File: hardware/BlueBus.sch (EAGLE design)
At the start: 72 parts

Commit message: [FIX] hardware: BlueBus v7 * Update Silkscreen for Speaker outputs * Rewire Speaker negative outputs to support single ended operation without overheating * Place 10uF cap for TPA6017A2 near input of 5v so all VDDs can benefit from it * Connect TPA6017A2 N/C pin to GND * Move TPA6017A2 gain resistor * Rewire transient filter for BC127 on the 3.3v rail per application note * Update placement of several passives for alignment * Update passive names to move from bottom right to left, to top right to left * Update Silkscreen with GitHub address
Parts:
- removed R21: 240, Passives:240OHM
- added C28, C29: 0.47uF, Passives:0.47UF
- added C30: 4.7uF, Passives:4.7UF
- added C31: 100nF, Passives:100NF
- C1: value 0.1uF -> 100uF; device Passives:0.1UF -> Passives:100UF2917
- C10: value 47nF -> 0.1uF; device Passives:47NF -> Passives:0.1UF
- C11: value 0.01uF -> 0.1uF; device Passives:0.01UF -> Passives:0.1UF
- C12: value 10uF -> 0.1uF; device Passives:10UF -> Passives:0.1UF
- C13: value 0.47uF -> 10uF; device Passives:0.47UF -> Passives:10UF
- C14, C16, C17, C18: value 0.47uF -> 0.1uF; device Passives:0.47UF -> Passives:0.1UF
- C15: value 10uF -> 2.2uF; device Passives:10UF -> Passives:2.2UF
- C19, C20: value 0.47uF -> (none); device Passives:0.47UF -> Passives:10UF2012
- C2: value 0.1uF -> 47nF; device Passives:0.1UF -> Passives:47NF
- C21: value 22uF -> (none); device Passives:22UF -> Passives:10UF2012
- C22, C23, C24, C27: value 0.1uF -> 0.47uF; device Passives:0.1UF -> Passives:0.47UF
- C25, C3: value 0.1uF -> 10uF; device Passives:0.1UF -> Passives:10UF
- C26: value 10uF -> 0.47uF; device Passives:10UF -> Passives:0.47UF
- C4: value 0.1uF -> 22uF; device Passives:0.1UF -> Passives:22UF
- C7: value 4.7uF -> 0.01uF; device Passives:4.7UF -> Passives:0.01UF
- C8: value 2.2uF -> 0.1uF; device Passives:2.2UF -> Passives:0.1UF
- C9: value 100uF -> 0.1uF; device Passives:100UF2917 -> Passives:0.1UF
- D3: value GREEN-0805 -> 2A/100V; device Seeed-LED:SMD-LED-CLEAR-GREEN(0805) -> Passives:SCHOTTKYDIODE2A30V
- D5: value RED-0805 -> GREEN-0805; device Seeed-LED:SMD-LED-CLEAR-RED(0805) -> Seeed-LED:SMD-LED-CLEAR-GREEN(0805)
- D6: value 2A/100V -> RED-0805; device Passives:SCHOTTKYDIODE2A30V -> Seeed-LED:SMD-LED-CLEAR-RED(0805)
- R1: value 0.22 -> 100k; device Passives:0.22OHM -> Passives:100KOHM0805
- R10: value 100k -> 10k; device Passives:100KOHM0805 -> Passives:10KOHM0805
- R11, R12: value 100k -> 1k; device Passives:100KOHM0805 -> Passives:1KOHM
- R13: value 100k -> 36k; device Passives:100KOHM0805 -> Passives:36KOHM2012
- R14: value 1k -> 2k; device Passives:1KOHM -> Passives:2KOHM0805
- R15: value 1k -> 100k; device Passives:1KOHM -> Passives:100KOHM0805
- R16: value 10k -> 100k; device Passives:10KOHM0805 -> Passives:100KOHM0805
- R17: value 5.1k -> 10k; device Passives:5.1KOHM0805 -> Passives:10KOHM0805
- R18: value 36k -> 10k; device Passives:36KOHM2012 -> Passives:10KOHM0805
- R19: value 2k -> 10k; device Passives:2KOHM0805 -> Passives:10KOHM0805
- R2: value 0.75 -> 47k; device Passives:0.75OHM -> Passives:47KOHM
- R3: value 10k -> 9.09k; device Passives:10KOHM0805 -> Passives:9.09KOHM
- R4: value 10k -> 2k; device Passives:10KOHM0805 -> Passives:2KOHM0805
- R5: value 10k -> 240; device Passives:10KOHM0805 -> Passives:240OHM
- R7: value 47k -> 5.1k; device Passives:47KOHM -> Passives:5.1KOHM0805
- R8: value 9.09k -> 100k; device Passives:9.09KOHM -> Passives:100KOHM0805
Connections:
- removed net BT_VBAT: BC127.VBAT, R1.2, R2.1
- removed net SPKR_OUT_NEG: SPKR_OUT.2, SPKR_OUT.4, TPA6017A2.LOUT-, TPA6017A2.ROUT-
- removed net VBAT_CAP: C7.1, R1.1
- new net BT_VCHG: BC127.VCHG, C30.1, R4.1
- new net SPKR_OUT_GND: C19.2, C20.2, C21.2, SPKR_OUT.3, SPKR_OUT.4
- new net SPKR_OUT_LN: C21.1, TPA6017A2.LOUT-
- new net SPKR_OUT_RN: C19.1, TPA6017A2.ROUT-
- net 3.3V: now also BC127.VBAT, C10.1, C11.1, C16.1, C17.1, C18.1, C31.1, C8.1, C9.1, D6.+, R10.1, R17.1, R19.2, R4.2, R7.2, R8.1, R9.1; no longer BC127.VCHG, C1.1, C2.1, C22.1, C23.1, C24.1, C3.1, C4.1, D4.+, R12.1, R13.1, R16.1, R17.2, R2.2, R20.1, R3.2
- net 5V: now also C22.1, C23.1, C25.1, C4.1, D3.C, R15.1, R16.2, R2.1, R20.2; no longer C13.1, C14.1, C15.1, C21.1, D6.C, R10.1, R11.2, R4.2, R7.1
- net BS: now also C7.2; no longer C11.2
- net BT_RESET: now also R17.2; no longer R6.2
- net BT_URX: now also R18.1, R18.2; no longer R5.1, R5.2
- net BT_UTX: now also R19.1, R20.1; no longer R3.1, R4.1
- net BYP: now also C24.1; no longer C20.1
- net EE_CS: now also R7.1; no longer R17.1
- net EN: now also R1.2; no longer R9.2
- net FB: now also R2.2, R3.2; no longer R7.2, R8.2
- net GAIN1: now also R15.2; no longer R10.2
- net GND: now also C11.2, C16.2, C17.2, C18.2, C20.1, C30.2, C31.2, R14.2, R3.1, TPA6017A2.NC; no longer C20.2, C21.2, C26.2, C27.2, C7.2, R19.2, R8.1
- net MCP_5V: now also D3.A; no longer D6.A
- net MCP_LED0: now also R12.1; no longer R15.1
- net MCP_LED0_RES: now also D6.-, R12.2; no longer D5.-, R15.2
- net MCP_LED1: now also R11.1; no longer R14.1
- net MCP_LED1_RES: now also D5.-, R11.2; no longer D4.-, R14.2
- net MCP_RESET: now also R10.2; no longer R16.2
- net MCU_MCLR: now also R5.2; no longer R21.2
- net MCU_MCLR_PULL_UP: now also C12.1, R5.1, R6.2; no longer C27.1, R20.2, R21.1
- net ON_LED: now also D4.+, R13.1; no longer D3.+, R18.1
- net ON_LED_RES: now also D4.-, R13.2, R14.1; no longer D3.-, R18.2, R19.1
- net SHDN: now also R16.1; no longer R11.1
- net SPKR_IN_LN: now also C27.1, C27.2; no longer C16.1, C16.2
- net SPKR_IN_LP: now also C28.1, C28.2; no longer C18.1, C18.2
- net SPKR_IN_RN: now also C26.1, C26.2; no longer C19.1, C19.2
- net SPKR_IN_RP: now also C29.1, C29.2; no longer C17.1, C17.2
- net SPKR_OUT_RP: now also SPKR_OUT.2; no longer SPKR_OUT.3
- net SW: now also C7.1; no longer C11.1
- net SYS_URX: now also R8.2; no longer R13.2
- net SYS_UTX: now also R9.2; no longer R12.2
- net VCAP: now also C13.1, C14.1; no longer C25.1, C26.1
- net VIN: now also C1.1, C2.1, C3.1, R1.1; no longer C10.1, C12.1, C9.1, R9.1
- net VTR: now also C15.1; no longer C8.1

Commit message: [IMP] hardware: BlueBus Rev A * Remove TPA6017A2 in favor of PCM5102A Line Level DAC which will fix quality issues * Completely new layout of board and schematic * Update Silkscreen to use vector fonts of consistent sizes * Resize board to 45mm x 70mm from 55mm x 90mm * Update design of transient filter to prevent voltage drops at boot * Add DSP Output SMB connector * Add circuit for mono microphone input * Add 1.5A Littleblock Fuse to prevent over-current * Miter board corners for rounded look
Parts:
- removed FRAME3: FRAME-LETTER, Frame:FRAME-LETTER
- removed JP1: (no value), pinhead:PINHD-1X3/90
- removed R20: 10k, Passives:10KOHM0805
- removed TPA6017A2: (no value), TPA6017A2:TPA6017A2
- added DSP_OUT: SMB_CONN, Connectors:SMB_CONN
- added F1: 1.5A, Passives:LITTLEBLOCK_FUSE_15A
- added PCM5102A: PCM5102A, ICs:PCM5102A
- added PWR: (no value), SparkFun-Connectors:CONN_03
- added SH1, SH2: SHORTT5, shorts:SHORTT5
- BC127: device BC127:BC127 -> ICs:BC127
- BT_UART: device SparkFun-Connectors:CONN_05 -> SparkFun-Connectors:CONN_03
- C1: value 100uF -> 1uF; device Passives:100UF2917 -> Passives:1UF
- C12: value 0.1uF -> 2.2uF; device Passives:0.1UF -> Passives:2.2UF
- C13: value 10uF -> 47nF; device Passives:10UF -> Passives:47NF
- C14: value 0.1uF -> 10uF; device Passives:0.1UF -> Passives:10UF
- C15: value 2.2uF -> 0.1uF; device Passives:2.2UF -> Passives:0.1UF
- C18: value 0.1uF -> 2.2nF; device Passives:0.1UF -> Passives:2.2NF
- C19: value (none) -> 10uF
- C2: value 47nF -> 0.01uF; device Passives:47NF -> Passives:0.01UF
- C20: value (none) -> 2.2uF; device Passives:10UF2012 -> Passives:2.2UF
- C21: value (none) -> 0.1uF; device Passives:10UF2012 -> Passives:0.1UF
- C22: value 0.47uF -> 2.2nF; device Passives:0.47UF -> Passives:2.2NF
- C23: value 0.47uF -> 2.2uF; device Passives:0.47UF -> Passives:2.2UF
- C24, C26, C28: value 0.47uF -> 0.1uF; device Passives:0.47UF -> Passives:0.1UF
- C25: device Passives:10UF -> Passives:10UF2012
- C27, C29: value 0.47uF -> 10uF; device Passives:0.47UF -> Passives:10UF2012
- C30: value 4.7uF -> 0.1uF; device Passives:4.7UF -> Passives:0.1UF
- C31: value 100nF -> 4.7uF; device Passives:100NF -> Passives:4.7UF
- C4: value 22uF -> 100uF; device Passives:22UF -> Passives:100UF2917
- C6: value 2.2uF -> 22uF; device Passives:2.2UF -> Passives:22UF
- C7: value 0.01uF -> 0.1uF; device Passives:0.01UF -> Passives:0.1UF
- D4, D5: value GREEN-0805 -> LED_GREEN; device Seeed-LED:SMD-LED-CLEAR-GREEN(0805) -> Passives:LED_GREEN
- D6: value RED-0805 -> LED_RED; device Seeed-LED:SMD-LED-CLEAR-RED(0805) -> Passives:LED_RED
- MIC_IN: device SparkFun-Connectors:CONN_03 -> SparkFun-Connectors:CONN_02
- PIC24FJ1024GA606: device PIC24FJ1024GA606:PIC24FJ1024GA606 -> ICs:PIC24FJ1024GA606
- R1: value 100k -> 47k; device Passives:100KOHM0805 -> Passives:47KOHM
- R10: device Passives:10KOHM0805 -> Passives:10KOHM
- R13: value 36k -> 1k; device Passives:36KOHM2012 -> Passives:1KOHM
- R14: value 2k -> 470; device Passives:2KOHM0805 -> Passives:470OHM
- R15: value 100k -> 470; device Passives:100KOHM0805 -> Passives:470OHM
- R16, R8, R9: value 100k -> 10k; device Passives:100KOHM0805 -> Passives:10KOHM
- R17: value 10k -> 240; device Passives:10KOHM0805 -> Passives:240OHM
- R18: value 10k -> 2; device Passives:10KOHM0805 -> Passives:2OHM
- R19: value 10k -> 2k; device Passives:10KOHM0805 -> Passives:2KOHM
- R2: value 47k -> 9.09k; device Passives:47KOHM -> Passives:9.09KOHM
- R3: value 9.09k -> 100k; device Passives:9.09KOHM -> Passives:100KOHM
- R4: value 2k -> 5.1k; device Passives:2KOHM0805 -> Passives:5.1KOHM
- R5: value 240 -> 100k; device Passives:240OHM -> Passives:100KOHM
- R6: value 10k -> 100k; device Passives:10KOHM0805 -> Passives:100KOHM
- R7: value 5.1k -> 10k; device Passives:5.1KOHM0805 -> Passives:10KOHM
- SPKR_OUT: value (none) -> FEMALE 2x3; device pinhead:PINHD-2X3/90 -> SparkFun-Connectors:CONN_03X2FEMALE
- TH3122: device TH3122_4:TH3122.4 -> ICs:TH3122.4
- XC6210: device XC6210:XC6210SOT25 -> ICs:XC6210SOT25
- XRP7659: device XRP7659:XRP7659SOT23-6 -> ICs:XRP7659SOT23-6
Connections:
- net MCP_5V renamed 5V_USB
- removed net BS: C7.2, XRP7659.BS
- removed net BT_RESET: BC127.RST#, PIC24FJ1024GA606.PGED3/AN4/C1INB/RP28/OCM3B/RB4, R17.2
- removed net BT_VCHG: BC127.VCHG, C30.1, R4.1
- removed net BYP: C24.1, TPA6017A2.BYPASS
- removed net EN: R1.2, XRP7659.EN
- removed net FB: R2.2, R3.2, XRP7659.FB
- removed net GAIN1: R15.2, TPA6017A2.GAIN1
- removed net MCP_LED0: MCP2221A.GP0, R12.1
- removed net MCP_LED0_RES: D6.-, R12.2
- removed net MCP_LED1: MCP2221A.GP1, R11.1
- removed net MCP_LED1_RES: D5.-, R11.2
- removed net MCP_RESET: MCP2221A.RST, R10.2
- removed net MCU_MCLR_PULL_UP: C12.1, R5.1, R6.2
- removed net MIC_LP: BC127.MIC_LP, MIC_IN.1
- removed net MIC_NEG: BC127.MIC_LN, BC127.MIC_RN, MIC_IN.3
- removed net MIC_RP: BC127.MIC_RP, MIC_IN.2
- removed net ON_LED: D4.+, PIC24FJ1024GA606.PMD0/RE0, R13.1
- removed net ON_LED_RES: D4.-, R13.2, R14.1
- removed net SHDN: R16.1, TPA6017A2.SHUTDOWN
- removed net SPKR_IN_LN: BC127.SPKR_LN, C27.1, C27.2, TPA6017A2.LIN-
- removed net SPKR_IN_LP: BC127.SPKR_LP, C28.1, C28.2, TPA6017A2.LIN+
- removed net SPKR_IN_RN: BC127.SPKR_RN, C26.1, C26.2, TPA6017A2.RIN-
- removed net SPKR_IN_RP: BC127.SPKR_RP, C29.1, C29.2, TPA6017A2.RIN+
- removed net SPKR_OUT_GND: C19.2, C20.2, C21.2, SPKR_OUT.3, SPKR_OUT.4
- removed net SPKR_OUT_LN: C21.1, TPA6017A2.LOUT-
- removed net SPKR_OUT_LP: SPKR_OUT.1, TPA6017A2.LOUT+
- removed net SPKR_OUT_RN: C19.1, TPA6017A2.ROUT-
- removed net SPKR_OUT_RP: SPKR_OUT.2, TPA6017A2.ROUT+
- removed net SW: C7.1, D2.C, L1.1, XRP7659.SW
- removed net VCAP: C13.1, C14.1, PIC24FJ1024GA606.VCAP
- new net 12V: D1.A, PWR.2
- new net 5VREG_BS: C2.1, XRP7659.BS
- new net 5VREG_EN: R3.2, XRP7659.EN
- new net 5VREG_FB: R1.1, R2.1, XRP7659.FB
- new net 5VREG_SW: C2.2, D2.C, L1.1, XRP7659.SW
- new net AGND: C24.2, C25.2, PCM5102A.AGND, SH1.P$2, SPKR_OUT.3, SPKR_OUT.4
- new net BT_3V3_FILTER: BC127.VCHG, C31.1, R18.1
- new net BT_DCLK: BC127.PCM1_CLK, PCM5102A.BCK
- new net BT_DOUT: BC127.PCM1_OUT, DSP_OUT.1, PCM5102A.DIN
- new net BT_DWS: BC127.PCM1_SYNC, PCM5102A.LRCK
- new net BT_MIC_BIAS: BC127.MIC_BIAS, R19.2
- new net BT_MIC_RN: BC127.MIC_RN, MIC_IN.2
- new net BT_MIC_RP: BC127.MIC_RP, MIC_IN.1, R19.1
- new net BT_RST: BC127.RST#, R10.1
- new net BT_VREGEN: BC127.VREGEN, PIC24FJ1024GA606.SDA3/IC6/PMD7/RE7
- new net DAC_CAPM: C20.2, PCM5102A.CAPM
- new net DAC_CAPP: C20.1, PCM5102A.CAPP
- new net DAC_OUT_L: PCM5102A.OUTL, R14.2
- new net DAC_OUT_R: PCM5102A.OUTR, R15.2
- new net DAC_VNEG: C23.1, PCM5102A.VNEG
- new net DGND: C26.2, C27.2, PCM5102A.DGND, SH2.P$2
- new net MCP_RST: MCP2221A.RST, R9.2
- new net MCP_RX_LED: MCP2221A.GP1, R12.1
- new net MCP_RX_LED_RES: D6.C, R13.2
- new net MCP_TX_LED: MCP2221A.GP0, R13.1
- new net MCP_TX_LED_RES: D5.C, R12.2
- new net MCU_MCLR_RES: C30.1, R16.2, R17.1
- new net MCU_ON_LED: PIC24FJ1024GA606.PMD0/RE0, R11.1
- new net MCU_ON_LED_RES: D4.A, R11.2
- new net MCU_VCAP: C14.1, C15.1, PIC24FJ1024GA606.VCAP
- new net SPKR_OUT_L: C18.1, R14.1, SPKR_OUT.1, SPKR_OUT.6
- new net SPKR_OUT_R: C22.1, R15.1, SPKR_OUT.2, SPKR_OUT.5
- net 3.3V: now also C10.2, C19.1, C21.1, C24.1, C25.1, C26.1, C27.1, C28.1, C29.1, C5.1, C7.2, C8.2, C9.2, D5.A, D6.A, PCM5102A.AVDD, PCM5102A.CPVDD, PCM5102A.DVDD, PCM5102A.FLT, PCM5102A.FMT, PCM5102A.LDOO, PCM5102A.XSMT, R10.2, R16.1, R18.2, R5.1; no longer C10.1, C18.1, C31.1, C6.1, C8.1, C9.1, D5.+, D6.+, R10.1, R17.1, R19.2, R8.1
- net 5V: now also BT_UART.1, C1.1, C6.1, R1.2; no longer BT_UART.3, C22.1, C23.1, C25.1, C4.1, C5.1, R15.1, R16.2, R2.1, R20.2, TPA6017A2.PVDD@1, TPA6017A2.PVDD@2, TPA6017A2.VDD
- net BT_URX: now also BT_UART.2, R8.1, R8.2; no longer BT_UART.4, R18.1, R18.2
- net BT_UTX: now also BT_UART.3, R7.1; no longer BT_UART.5, R19.1, R20.1
- net EE_CS: now also PIC24FJ1024GA606.CLC4OUT/RP2/U6RTS/U6BCLK/ICM5/RD8, R4.1; no longer PIC24FJ1024GA606.C1INC/C2INC/C3INC/RP27/OCM2B/PMA2/PMALU/RG9, R7.1
- net EE_SCK: now also PIC24FJ1024GA606.RP16/RF3; no longer PIC24FJ1024GA606.AN14/RP14/CTED5/CTPLS/PMA1/PMALH/RB14
- net EE_SI: now also PIC24FJ1024GA606.RP30/RF2; no longer PIC24FJ1024GA606.AN9/TMPR/RP9/T1CK/PMA7/RB9
- net EE_SO: now also PIC24FJ1024GA606.RP4/PMACK2/RD9; no longer PIC24FJ1024GA606.AN8/RP8/PWRGT/RB8
- net GND: now also C10.1, C19.2, C21.2, C28.2, C29.2, C7.1, C8.1, C9.1, D4.C, PCM5102A.CPGND, PCM5102A.DEMP, PWR.1, R2.2, SH1.P$1, SH2.P$1; no longer BT_UART.1, C10.2, C2.2, C20.1, C24.2, C25.2, C8.2, C9.2, JP1.1, R14.2, R3.1, TPA6017A2.GAIN0, TPA6017A2.GND@1, TPA6017A2.GND@2, TPA6017A2.GND@3, TPA6017A2.GND@4, TPA6017A2.NC
- net IBUS: now also PWR.3; no longer JP1.3
- net IBUS_URX: now also PIC24FJ1024GA606.RP12/PMA14/PMCS1/RD11; no longer PIC24FJ1024GA606.RP23/PMACK1/RD2
- net IBUS_USTA: now also PIC24FJ1024GA606.CLC3OUT/RP11/U6CTS/ICM6/RD0; no longer PIC24FJ1024GA606.RP22/ICM7/PMBE0/RD3
- net IBUS_UTX: now also PIC24FJ1024GA606.RP3/PMA15/PMCS2/RD10; no longer PIC24FJ1024GA606.RP24/U5TX/ICM4/RD1
- net MCU_MCLR: now also R17.2; no longer R5.2
- net SYS_URX: now also PIC24FJ1024GA606.RP23/PMACK1/RD2, R5.2; no longer PIC24FJ1024GA606.PGEC2/AN6/RP6/RB6, R8.2
- net SYS_UTX: now also PIC24FJ1024GA606.RP24/U5TX/ICM4/RD1, R6.2; no longer PIC24FJ1024GA606.PGED2/AN7/RP7/U6TX/RB7, R9.2
- net VIN: now also C13.1, C4.1, F1.IN, F1.OUT, R3.1; no longer C1.1, C2.1, D1.A, JP1.2, R1.1
- net VTR: now also C12.1; no longer C15.1
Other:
- note added: "Audio DAC"
- note added: "SYSTEM UART"
- note removed: "Audio Amplifier"
- note removed: "Gain Setting"
- note removed: "System UART"

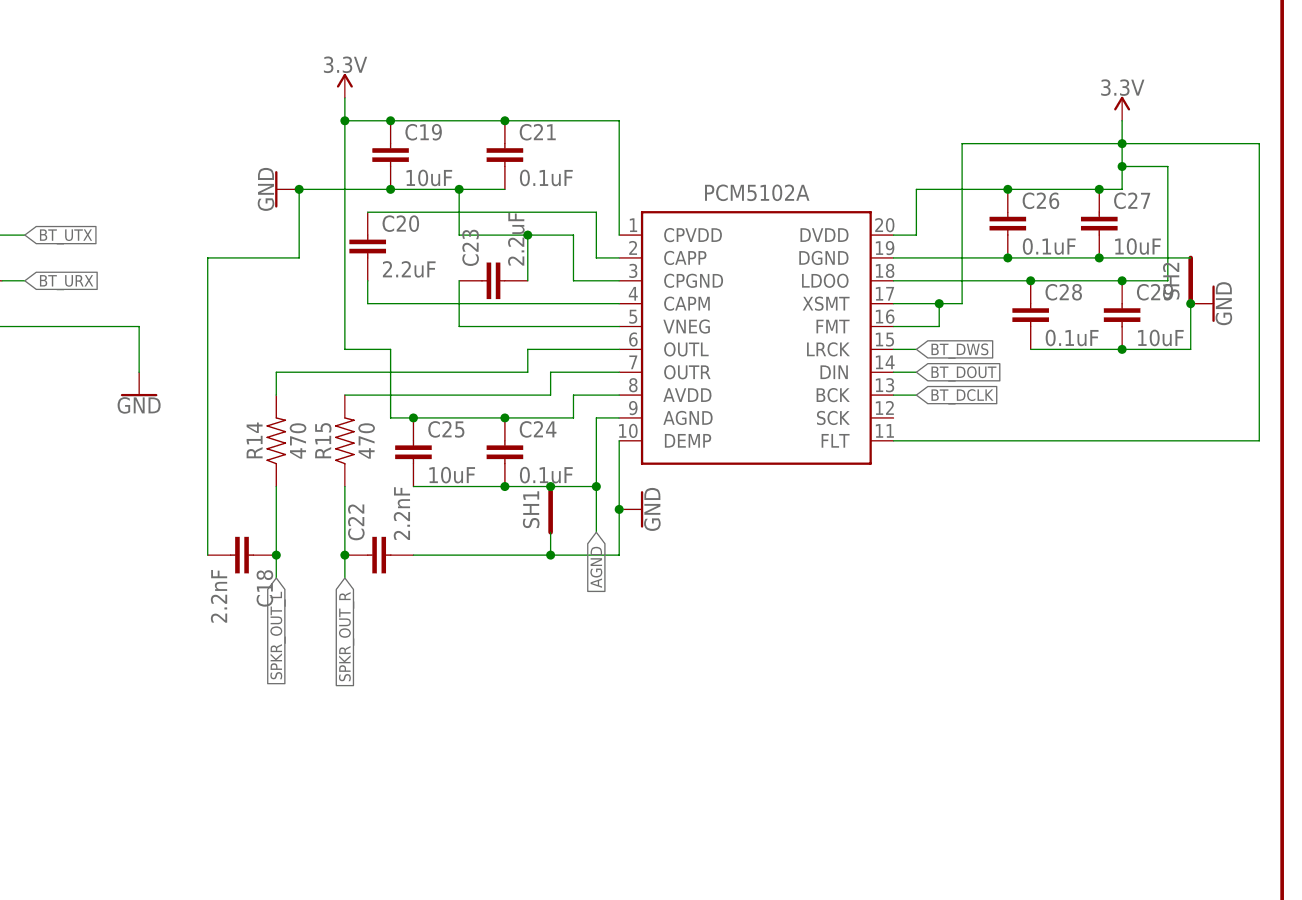
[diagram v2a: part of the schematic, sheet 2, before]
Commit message: [IMP] hardware: BlueBus Rev A * Improve Silkscreen * Rewire a couple of nets to reduce via count * Move passives into better alignment
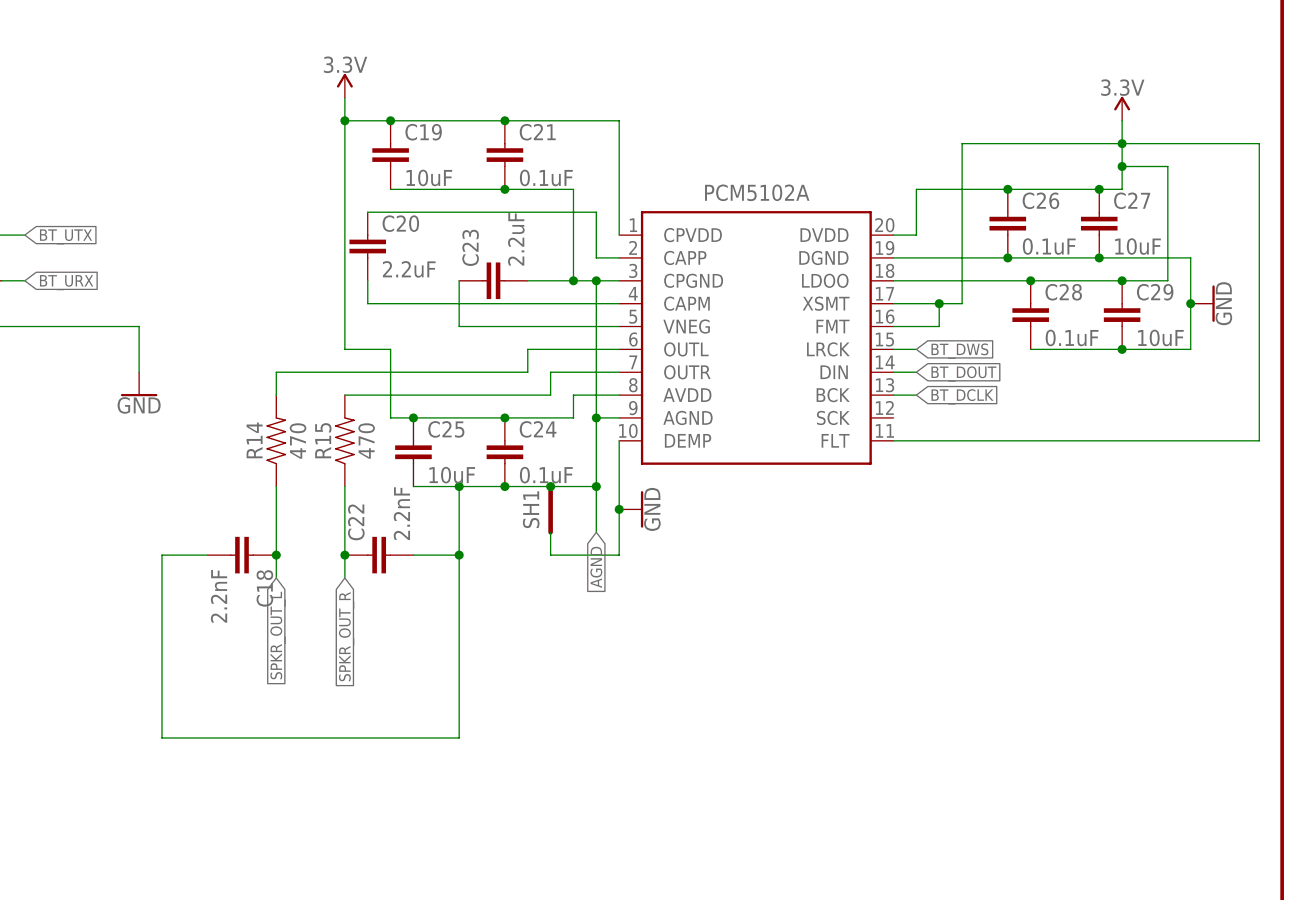
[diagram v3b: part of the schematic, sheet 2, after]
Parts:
- removed D4: LED_GREEN, Passives:LED_GREEN
- removed SH2: SHORTT5, shorts:SHORTT5
- added PWR_IN: (no value), SparkFun-Connectors:CONN_03
- PWR: value (none) -> LED_GREEN; device SparkFun-Connectors:CONN_03 -> Passives:LED_GREEN
- renumbered D5 to RX, D6 to TX, J1 to USB
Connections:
- removed net DGND: C26.2, C27.2, PCM5102A.DGND, SH2.P$2
- net 12V: now also PWR_IN.2; no longer PWR.2
- net AGND: now also C18.2, C19.2, C21.2, C22.2, C23.2, PCM5102A.CPGND
- net GND: now also C26.2, C27.2, PCM5102A.DGND, PWR.C, PWR_IN.1; no longer C18.2, C19.2, C21.2, C22.2, C23.2, D4.C, PCM5102A.CPGND, PWR.1, SH2.P$1
- net IBUS: now also PWR_IN.3; no longer PWR.3
- net MCU_ON_LED_RES: now also PWR.A; no longer D4.A
